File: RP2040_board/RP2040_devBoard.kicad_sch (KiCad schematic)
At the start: 33 parts, among them J1 USB_B_Micro, J2 Conn_01x21_Male, J3 Conn_01x21_Male, SW1 SW_Push, U1 RP2040, U2 AMS1117, U3 W25Q128JVS, Y1 Crystal

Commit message: SCH: added the respective footpriont for all of the pieces, but not definitive footprint
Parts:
- C1, C10, C11, C12, C13, C14, C15, C16, C2, C3, C4, C5, C6, C7, C8, C9: footprint (none) -> Capacitor_SMD:C_0805_2012Metric_Pad1.18x1.45mm_HandSolder
- D1, D2: footprint (none) -> LED_SMD:LED_1206_3216Metric_Pad1.42x1.75mm_HandSolder
- J1: footprint (none) -> Connector_USB:USB_Micro-B_Amphenol_10118194_Horizontal
- J2, J3: footprint (none) -> Connector_PinHeader_1.27mm:PinHeader_1x21_P1.27mm_Vertical
- R1, R2, R3, R4, R5, R6, R7: footprint (none) -> Resistor_SMD:R_0805_2012Metric_Pad1.20x1.40mm_HandSolder
- SW1: footprint (none) -> Connector_PinHeader_1.27mm:PinHeader_1x02_P1.27mm_Vertical
- Y1: footprint (none) -> Crystal:Crystal_SMD_SeikoEpson_MA505-2Pin_12.7x5.1mm_HandSoldering

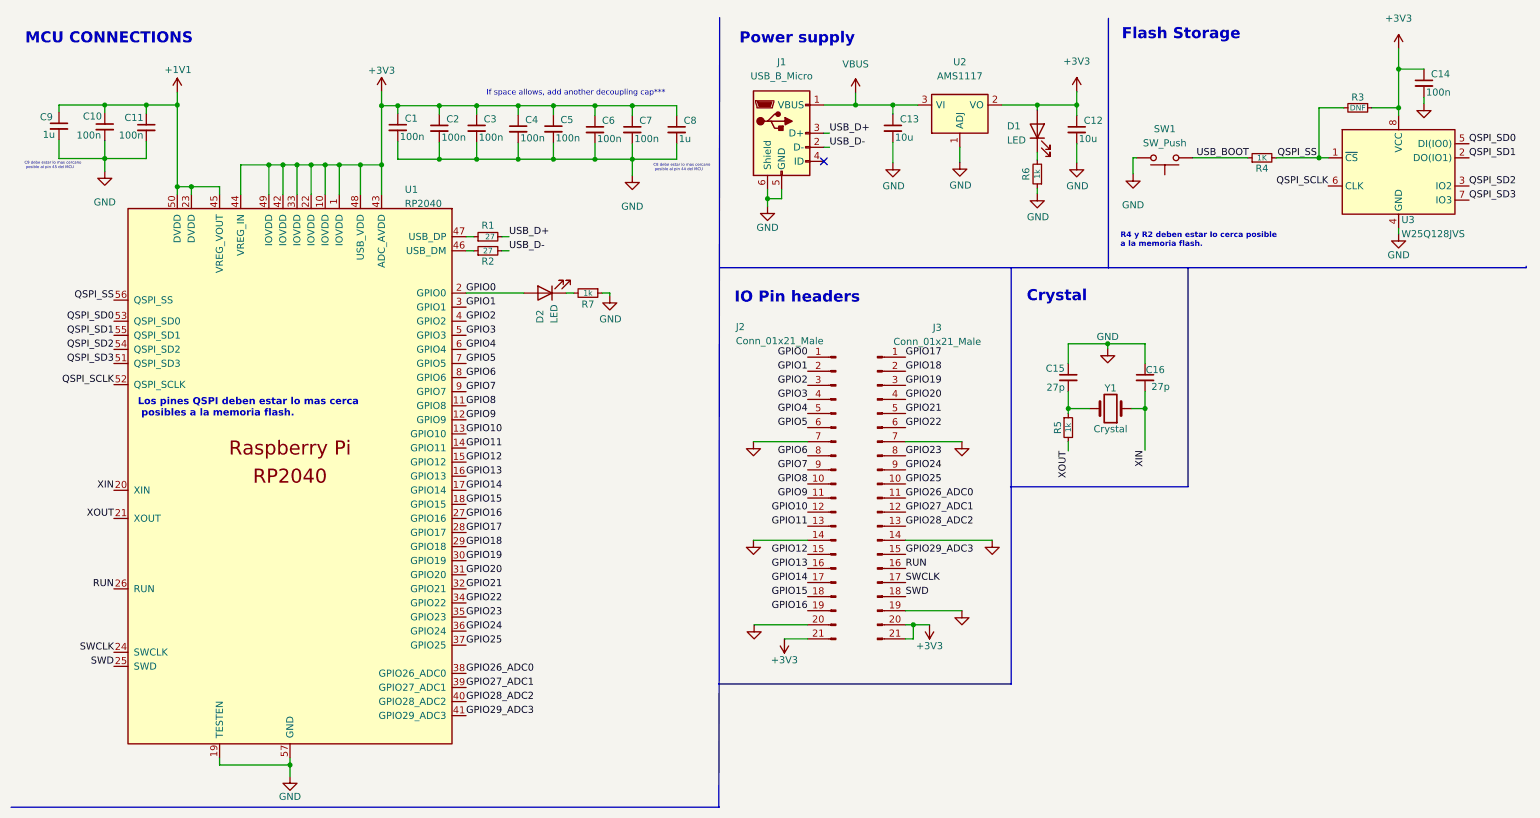
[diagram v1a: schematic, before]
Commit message: PCB: finished the layout, added the logos, labels for each pin.
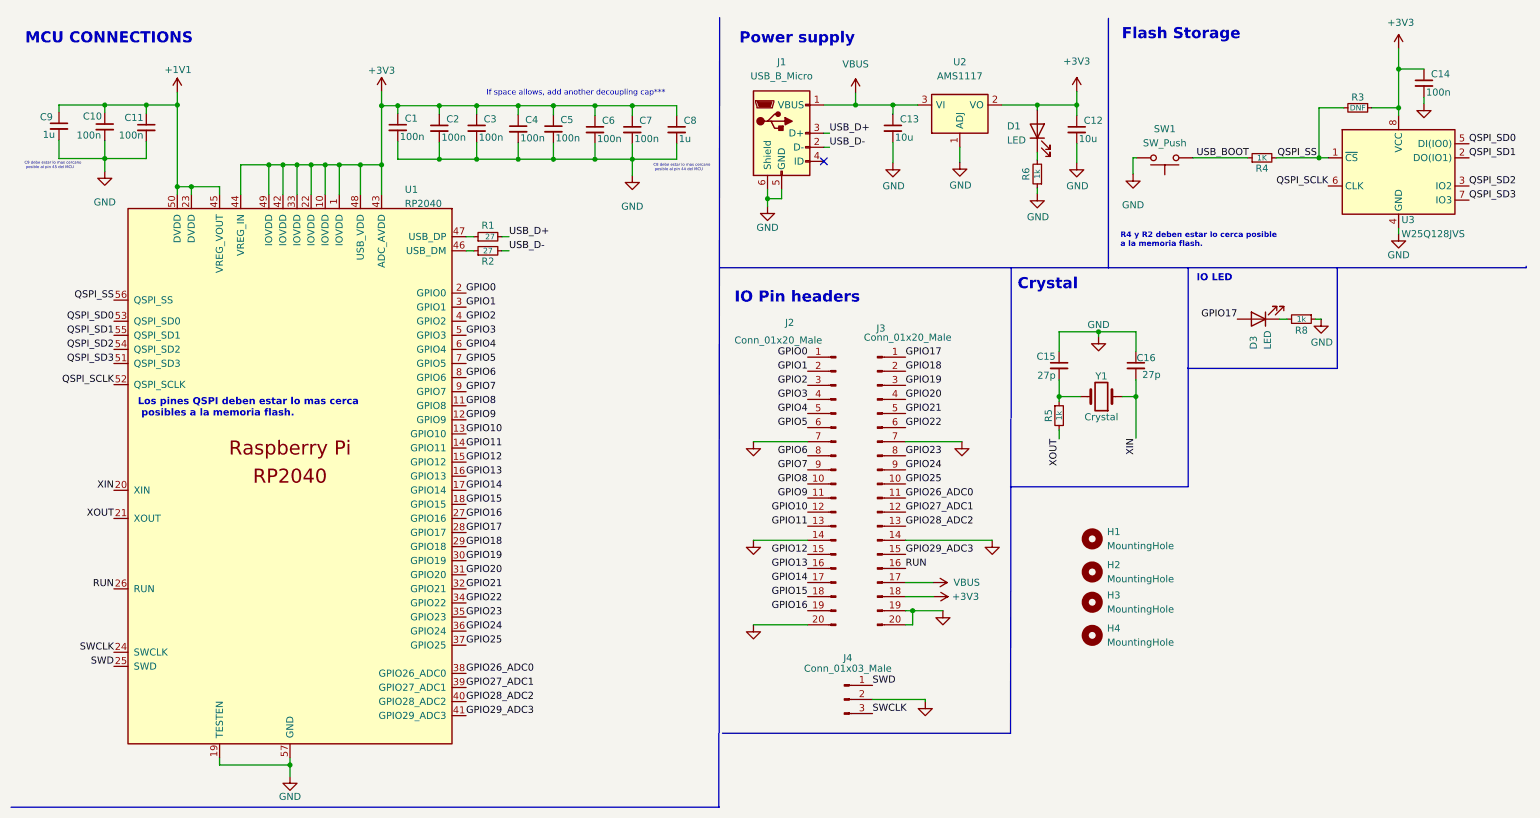
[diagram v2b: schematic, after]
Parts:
- removed D2: LED, LED_SMD:LED_1206_3216Metric_Pad1.42x1.75mm_HandSolder, symbol Device:LED
- removed J2, J3: Conn_01x21_Male, Connector_PinHeader_1.27mm:PinHeader_1x21_P1.27mm_Vertical, symbol Connector:Conn_01x21_Male
- removed R7: 1k, Resistor_SMD:R_0805_2012Metric_Pad1.20x1.40mm_HandSolder, symbol Device:R_Small
- added D3: LED, LED_SMD:LED_1206_3216Metric, symbol Device:LED
- added H1, H2, H3, H4: MountingHole, MountingHole:MountingHole_2.1mm, symbol Mechanical:MountingHole
- added J2, J3: Conn_01x20_Male, Connector_PinHeader_2.54mm:PinHeader_1x20_P2.54mm_Vertical, symbol Connector:Conn_01x20_Male
- added J4: Conn_01x03_Male, Connector_PinHeader_2.54mm:PinHeader_1x03_P2.54mm_Vertical, symbol Connector:Conn_01x03_Male
- added R8: 1k, Resistor_SMD:R_0603_1608Metric, symbol Device:R_Small
- C1, C10, C11, C12, C13, C14, C15, C16, C2, C3, C4, C5, C6, C7, C8, C9: footprint Capacitor_SMD:C_0805_2012Metric_Pad1.18x1.45mm_HandSolder -> Capacitor_SMD:C_0603_1608Metric
- D1: footprint LED_SMD:LED_1206_3216Metric_Pad1.42x1.75mm_HandSolder -> LED_SMD:LED_1206_3216Metric
- R1, R2, R3, R4, R5, R6: footprint Resistor_SMD:R_0805_2012Metric_Pad1.20x1.40mm_HandSolder -> Resistor_SMD:R_0603_1608Metric
- SW1: footprint Connector_PinHeader_1.27mm:PinHeader_1x02_P1.27mm_Vertical -> Tactile_SW:SW_PTS636_SMT-G_5_CNK
- U1: footprint RP2040_minimal:RP2040-QFN-56 -> MCU_RaspberryPi_and_Boards:RP2040-QFN-56
- Y1: footprint Crystal:Crystal_SMD_SeikoEpson_MA505-2Pin_12.7x5.1mm_HandSoldering -> Crystal:Crystal_SMD_HC49-SD
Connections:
- net +3V3: now also J3.18 (Pin_18)
- net GND: now also J2.14 (Pin_14), J2.20 (Pin_20), J2.7 (Pin_7), J3.14 (Pin_14), J3.19 (Pin_19), J3.20 (Pin_20), J3.7 (Pin_7), J4.2 (Pin_2), R8.1
- net GPIO0: now also J2.1 (Pin_1)
- net GPIO1: now also J2.2 (Pin_2)
- net GPIO10: now also J2.12 (Pin_12)
- net GPIO11: now also J2.13 (Pin_13)
- net GPIO12: now also J2.15 (Pin_15)
- net GPIO13: now also J2.16 (Pin_16)
- net GPIO14: now also J2.17 (Pin_17)
- net GPIO15: now also J2.18 (Pin_18)
- net GPIO16: now also J2.19 (Pin_19)
- net GPIO17: now also D3.2 (A), J3.1 (Pin_1)
- net GPIO18: now also J3.2 (Pin_2)
- net GPIO19: now also J3.3 (Pin_3)
- net GPIO2: now also J2.3 (Pin_3)
- net GPIO20: now also J3.4 (Pin_4)
- net GPIO21: now also J3.5 (Pin_5)
- net GPIO22: now also J3.6 (Pin_6)
- net GPIO23: now also J3.8 (Pin_8)
- net GPIO24: now also J3.9 (Pin_9)
- net GPIO25: now also J3.10 (Pin_10)
- net GPIO26_ADC0: now also J3.11 (Pin_11)
- net GPIO27_ADC1: now also J3.12 (Pin_12)
- net GPIO28_ADC2: now also J3.13 (Pin_13)
- net GPIO29_ADC3: now also J3.15 (Pin_15)
- net GPIO3: now also J2.4 (Pin_4)
- net GPIO4: now also J2.5 (Pin_5)
- net GPIO5: now also J2.6 (Pin_6)
- net GPIO6: now also J2.8 (Pin_8)
- net GPIO7: now also J2.9 (Pin_9)
- net GPIO8: now also J2.10 (Pin_10)
- net GPIO9: now also J2.11 (Pin_11)
- net RUN: now also J3.16 (Pin_16)
- net SWCLK: now also J4.3 (Pin_3)
- net SWD: now also J4.1 (Pin_1)
- net VBUS: now also J3.17 (Pin_17)
- new net: D3.1 (K), R8.2
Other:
- note added: "IO LED"
- moved on the sheet: C15, C16, R5, Y1

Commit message: board finish
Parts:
- removed SW1: SW_Push, Tactile_SW:SW_PTS636_SMT-G_5_CNK, symbol Switch:SW_Push
- added SW1: PTS815_SJM_250_SMTR_LFS, FOOTPRINTS_s1:SW4_PTS815 SJM 250 SMTR LFS_CNK, symbol PTS815:PTS815_SJM_250_SMTR_LFS
- D1, D3: footprint LED_SMD:LED_1206_3216Metric -> LED_SMD:LED_0603_1608Metric
- Y1: footprint Crystal:Crystal_SMD_HC49-SD -> MCU_RaspberryPi_and_Boards:Crystal_SMD_HC49-US
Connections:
- net GND: now also SW1.1
- net USB_BOOT: now also SW1.4
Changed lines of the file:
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@@
+    (stroke (width 0) (type default) (color 0 0 0 0))
+  )
+  (wire (pts (xy 214.249 37.338) (xy 215.2904 37.338))
     (stroke (width 0) (type default) (color 0 0 0 0))
   )
@@
     (stroke (width 0) (type default) (color 0 0 0 0))
   )
-  (wire (pts (xy 214.884 37.338) (xy 214.249 37.338))
-    (stroke (width 0) (type default) (color 0 0 0 0))
-  )
   (wire (pts (xy 164.211 27.813) (xy 170.942 27.813))
     (stroke (width 0) (type default) (color 0 0 0 0))
@@
     (stroke (width 0) (type default) (color 0 0 0 0))
   )
-  (wire (pts (xy 225.044 37.338) (xy 234.95 37.338))
+  (wire (pts (xy 225.4758 37.338) (xy 234.95 37.338))
     (stroke (width 0) (type default) (color 0 0 0 0))
   )
@@
       (effects (font (size 1.27 1.27)) (justify right))
     )
-    (property "Footprint" "LED_SMD:LED_1206_3216Metric" (id 2) (at 196.977 32.512 0)
+    (property "Footprint" "LED_SMD:LED_0603_1608Metric" (id 2) (at 196.977 32.512 0)
       (effects (font (size 1.27 1.27)) hide)
     )
@@
     (property "Reference" "Y1" (id 0) (at 208.534 76.708 0))
     (property "Value" "Crystal" (id 1) (at 208.534 84.074 0))
-    (property "Footprint" "Crystal:Crystal_SMD_HC49-SD" (id 2) (at 208.534 80.391 0)
+    (property "Footprint" "MCU_RaspberryPi_and_Boards:Crystal_SMD_HC49-US" (id 2) (at 208.534 80.391 0)
       (effects (font (size 1.27 1.27)) hide)
     )
@@
     )
   )
-  (symbol (lib_id "Switch:SW_Push") (at 219.964 37.338 0) (mirror x) (unit 1)
-    (in_bom yes) (on_board yes) (fields_autoplaced)
-    (property "Reference" "SW1" (id 0) (at 219.964 32.131 0))
-    (property "Value" "SW_Push" (id 1) (at 219.964 34.671 0))
-    (property "Footprint" "Tactile_SW:SW_PTS636_SMT-G_5_CNK" (id 2) (at 219.964 42.418 0)
-      (effects (font (size 1.27 1.27)) hide)
-    )
-    (property "Datasheet" "~" (id 3) (at 219.964 42.418 0)
-      (effects (font (size 1.27 1.27)) hide)
-    )
-    (pin "1")
-    (pin "2")
-  )
   (symbol (lib_id "power:GND") (at 183.388 88.519 0) (unit 1)
     (in_bom yes) (on_board yes)
@@
     (pin "1")
     (pin "2")
+  )
+  (symbol (lib_id "PTS815:PTS815_SJM_250_SMTR_LFS") (at 181.0766 32.3596 0) (unit 1)
+    (in_bom yes) (on_board yes) (fields_autoplaced)
+    (property "Reference" "SW1" (id 0) (at 220.3831 33.02 0)
+      (effects (font (size 1.524 1.524)))
+    )
+    (property "Value" "PTS815_SJM_250_SMTR_LFS" (id 1) (at 220.3831 32.2326 0)
+      (effects (font (size 1.524 1.524)) hide)
+    )
+    (property "Footprint" "FOOTPRINTS_s1:SW4_PTS815 SJM 250 SMTR LFS_CNK" (id 2) (at 219.5576 41.6052 0)
+      (effects (font (size 1.27 1.27) italic) hide)
+    )
+    (property "Datasheet" "PTS815 SJM 250 SMTR LFS" (id 3) (at 181.0766 32.3596 0)
+      (effects (font (size 1.27 1.27) italic) hide)
+    )
+    (pin "1")
+    (pin "4")
   )
   (symbol (lib_id "Connector:Conn_01x03_Male") (at 162.179 135.001 0) (unit 1)
@@
       (effects (font (size 1.27 1.27)) (justify right))
     )
-    (property "Footprint" "LED_SMD:LED_1206_3216Metric" (id 2) (at 236.855 66.421 0)
+    (property "Footprint" "LED_SMD:LED_0603_1608Metric" (id 2) (at 236.855 66.421 0)
       (effects (font (size 1.27 1.27)) hide)
     )
@@
     )
     (path "/1d380f75-9d96-4cb3-80b1-0161eae10300"
-      (reference "D1") (unit 1) (value "LED") (footprint "LED_SMD:LED_1206_3216Metric")
+      (reference "D1") (unit 1) (value "LED") (footprint "LED_SMD:LED_0603_1608Metric")
     )
     (path "/ee381a3f-e4a8-445d-97f7-36bc3fc74da6"
-      (reference "D3") (unit 1) (value "LED") (footprint "LED_SMD:LED_1206_3216Metric")
+      (reference "D3") (unit 1) (value "LED") (footprint "LED_SMD:LED_0603_1608Metric")
     )
     (path "/8305abe2-9ec2-40c5-b546-27ce019c1e90"
@@
       (reference "R8") (unit 1) (value "1k") (footprint "Resistor_SMD:R_0603_1608Metric")
     )
-    (path "/838cf614-b2e2-42f7-b700-9259c521d935"
-      (reference "SW1") (unit 1) (value "SW_Push") (footprint "Tactile_SW:SW_PTS636_SMT-G_5_CNK")
+    (path "/9e7bf311-c338-4c22-89d8-9b6c735a03ce"
+      (reference "SW1") (unit 1) (value "PTS815_SJM_250_SMTR_LFS") (footprint "FOOTPRINTS_s1:SW4_PTS815 SJM 250 SMTR LFS_CNK")
     )
     (path "/d94772be-f29e-4993-b418-3d2f2b018854"
@@
     )
     (path "/2d03d970-711c-47fd-8204-f3fce42059d8"
-      (reference "Y1") (unit 1) (value "Crystal") (footprint "Crystal:Crystal_SMD_HC49-SD")
-    )
-  )
+      (reference "Y1") (unit 1) (value "Crystal") (footprint "MCU_RaspberryPi_and_Boards:Crystal_SMD_HC49-US")
+    )
+  )
